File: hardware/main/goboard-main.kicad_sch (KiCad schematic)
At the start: 11 parts, among them J1 USB_C_Receptacle_USB2.0, J2 Conn_02x05_Top_Bottom, J3 Conn_01x01, J4 Conn_01x04, SW11 SW_Push, SW30 SW_DP3T

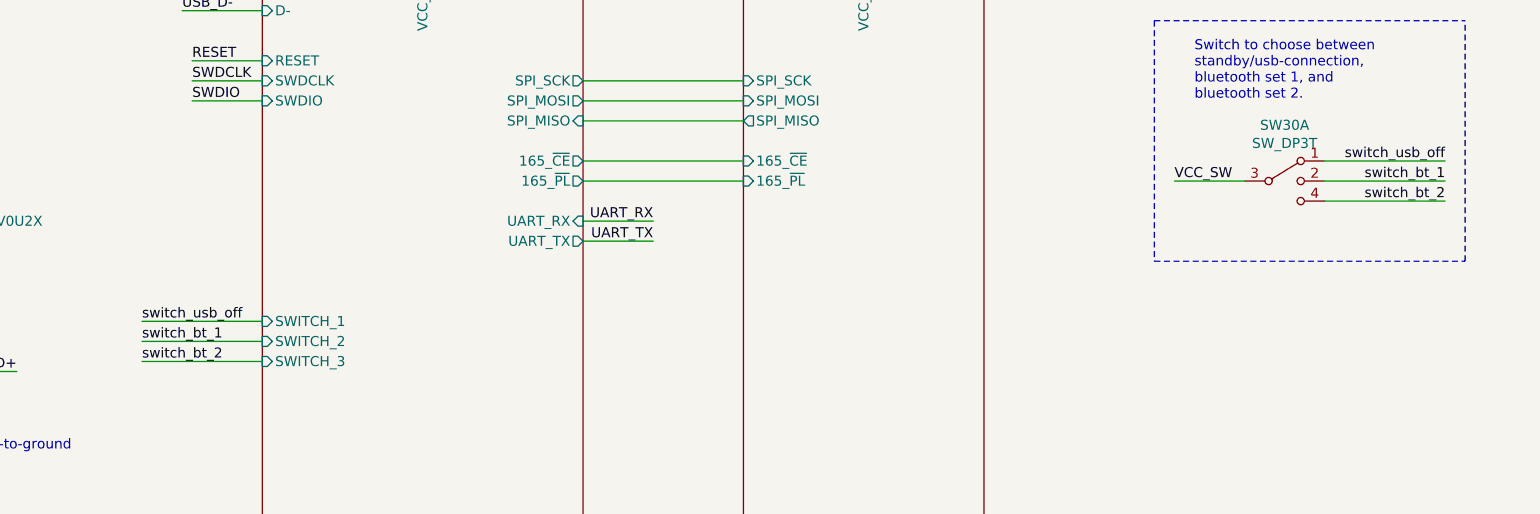
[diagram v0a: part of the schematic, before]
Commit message: Rework the off/bluetooth1/bluetooth2 switch connection
To save energy an external pull-down resistor is added and the off
position is not connected to the MCU.
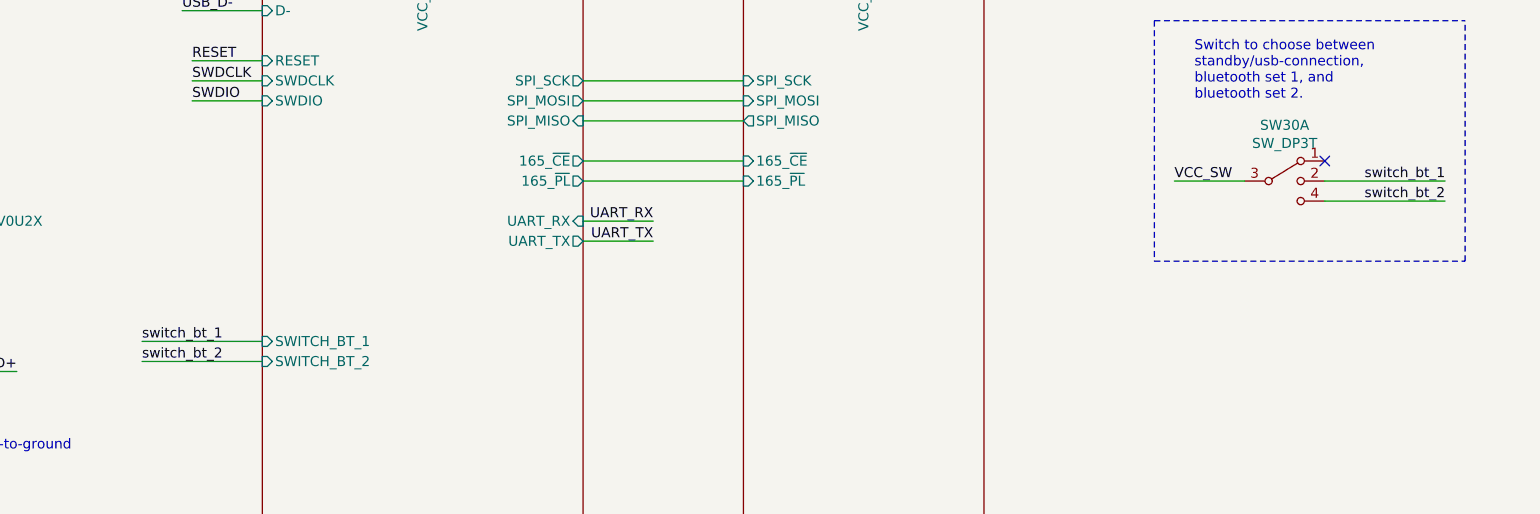
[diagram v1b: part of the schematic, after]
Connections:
- net switch_usb_off: no longer names the net of SW30.1
- no-connect marks 5 -> 6
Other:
- sheet MCU ports: added SWITCH_BT_1, SWITCH_BT_2; removed SWITCH_1, SWITCH_2, SWITCH_3
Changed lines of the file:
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@@
   (no_connect (at 41.91 66.04))
   (no_connect (at 45.72 165.1))
+  (no_connect (at 255.27 64.77))
   (wire (pts (xy 19.05 73.66) (xy 19.05 76.2))
     (stroke (width 0) (type solid) (color 0 0 0 0))
@@
     (stroke (width 0) (type solid) (color 0 0 0 0))
   )
-  (wire (pts (xy 105.41 85.09) (xy 120.65 85.09))
-    (stroke (width 0) (type solid) (color 0 0 0 0))
-  )
   (wire (pts (xy 105.41 87.63) (xy 120.65 87.63))
     (stroke (width 0) (type solid) (color 0 0 0 0))
@@
   )
   (wire (pts (xy 250.19 139.7) (xy 260.35 139.7))
-    (stroke (width 0) (type solid) (color 0 0 0 0))
-  )
-  (wire (pts (xy 255.27 64.77) (xy 270.51 64.77))
     (stroke (width 0) (type solid) (color 0 0 0 0))
   )
@@
     (effects (font (size 1.27 1.27)) (justify right bottom))
   )
-  (label "switch_usb_off" (at 105.41 85.09 0)
-    (effects (font (size 1.27 1.27)) (justify left bottom))
-  )
   (label "switch_bt_1" (at 105.41 87.63 0)
     (effects (font (size 1.27 1.27)) (justify left bottom))
@@
   (label "UART_TX" (at 250.19 139.7 0)
     (effects (font (size 1.27 1.27)) (justify left bottom))
-  )
-  (label "switch_usb_off" (at 270.51 64.77 180)
-    (effects (font (size 1.27 1.27)) (justify right bottom))
   )
   (label "switch_bt_1" (at 270.51 67.31 180)
@@
       (effects (font (size 1.27 1.27)) (justify right))
     )
-    (pin "SWITCH_1" input (at 120.65 85.09 180)
-      (effects (font (size 1.27 1.27)) (justify left))
-    )
-    (pin "SWITCH_2" input (at 120.65 87.63 180)
-      (effects (font (size 1.27 1.27)) (justify left))
-    )
-    (pin "SWITCH_3" input (at 120.65 90.17 180)
-      (effects (font (size 1.27 1.27)) (justify left))
-    )
     (pin "V_MID" input (at 120.65 111.76 180)
       (effects (font (size 1.27 1.27)) (justify left))
@@
     )
     (pin "CHARGE" output (at 120.65 134.62 180)
+      (effects (font (size 1.27 1.27)) (justify left))
+    )
+    (pin "SWITCH_BT_2" input (at 120.65 90.17 180)
+      (effects (font (size 1.27 1.27)) (justify left))
+    )
+    (pin "SWITCH_BT_1" input (at 120.65 87.63 180)
       (effects (font (size 1.27 1.27)) (justify left))
     )
@@
       (reference "#PWR0147") (unit 1) (value "+5V") (footprint "")
     )
+    (path "/d1d7b976-c206-4a6a-bf43-9e0a3d3fc0a5/cf9f8d8d-da0f-4591-b106-4ccbc5c13dc0"
+      (reference "#PWR0148") (unit 1) (value "GND") (footprint "")
+    )
+    (path "/d1d7b976-c206-4a6a-bf43-9e0a3d3fc0a5/020d5d8f-9949-4018-bf6f-14d0c6edcb95"
+      (reference "#PWR?") (unit 1) (value "GND") (footprint "")
+    )
     (path "/d1d7b976-c206-4a6a-bf43-9e0a3d3fc0a5/3b11a76b-0594-44ea-a5af-67b22af13aef"
       (reference "C1") (unit 1) (value "100nF") (footprint "Capacitor_SMD:C_0603_1608Metric_Pad1.08x0.95mm_HandSolder")
@@
       (reference "R24") (unit 1) (value "100k") (footprint "Resistor_SMD:R_0603_1608Metric_Pad0.98x0.95mm_HandSolder")
     )
+    (path "/d1d7b976-c206-4a6a-bf43-9e0a3d3fc0a5/f9d78325-6fa2-4c37-ba1e-b9fa566c985f"
+      (reference "R25") (unit 1) (value "100k") (footprint "Resistor_SMD:R_0603_1608Metric_Pad0.98x0.95mm_HandSolder")
+    )
+    (path "/d1d7b976-c206-4a6a-bf43-9e0a3d3fc0a5/3a9f3330-4728-47be-a54c-1662ecaf0122"
+      (reference "R26") (unit 1) (value "100k") (footprint "Resistor_SMD:R_0603_1608Metric_Pad0.98x0.95mm_HandSolder")
+    )
     (path "/d1d7b976-c206-4a6a-bf43-9e0a3d3fc0a5/ab5a7c2d-c6f5-4633-a330-435b31021904"

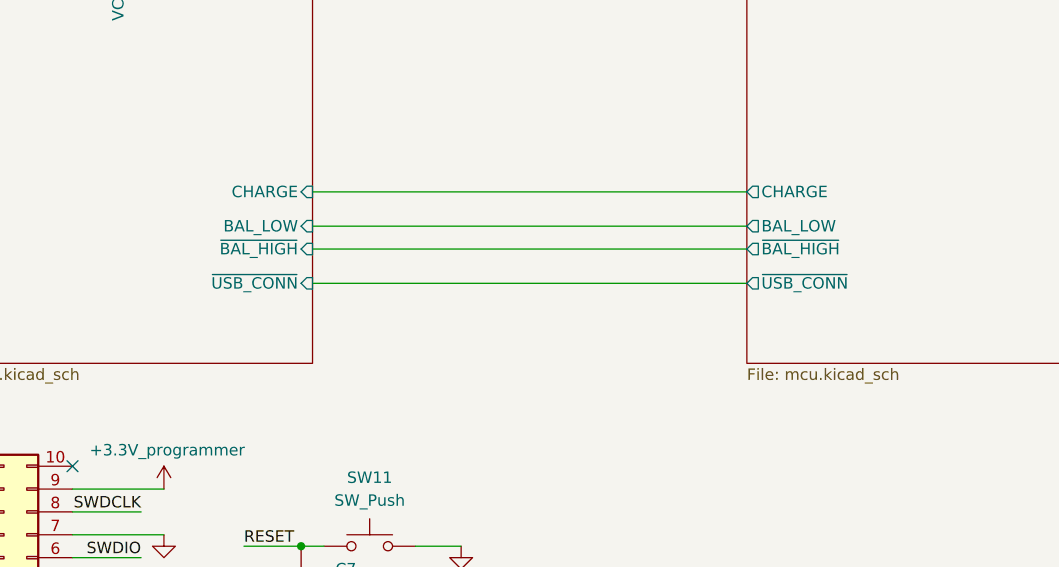
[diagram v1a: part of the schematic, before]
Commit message: Remove the USB sense curcuit
As V_BUS is connected to the MCU it can detect when the USB is
connected.
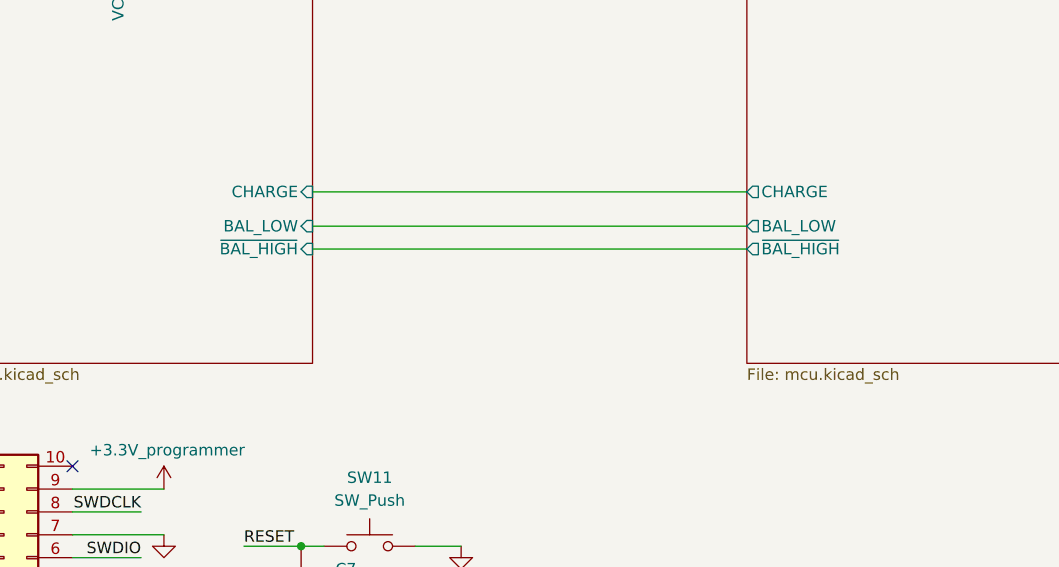
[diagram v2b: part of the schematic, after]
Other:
- sheet MCU ports: added none; removed ~USB_CONN
- sheet Power Supply ports: added none; removed ~USB_CONN
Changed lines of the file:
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@@
-    (stroke (width 0) (type solid) (color 0 0 0 0))
-  )
-  (wire (pts (xy 72.39 144.78) (xy 120.65 144.78))
     (stroke (width 0) (type solid) (color 0 0 0 0))
   )
@@
       (effects (font (size 1.27 1.27)) (justify left))
     )
-    (pin "~USB_CONN" output (at 120.65 144.78 180)
-      (effects (font (size 1.27 1.27)) (justify left))
-    )
     (pin "CHARGE" output (at 120.65 134.62 180)
       (effects (font (size 1.27 1.27)) (justify left))
@@
       (effects (font (size 1.27 1.27)) (justify right))
     )
-    (pin "~USB_CONN" input (at 72.39 144.78 0)
-      (effects (font (size 1.27 1.27)) (justify right))
-    )
     (pin "VCC_SW" output (at 50.8 106.68 90)
       (effects (font (size 1.27 1.27)) (justify right))
@@
     )
     (path "/d1d7b976-c206-4a6a-bf43-9e0a3d3fc0a5/020d5d8f-9949-4018-bf6f-14d0c6edcb95"
-      (reference "#PWR?") (unit 1) (value "GND") (footprint "")
+      (reference "#PWR0149") (unit 1) (value "GND") (footprint "")
     )
     (path "/d1d7b976-c206-4a6a-bf43-9e0a3d3fc0a5/3b11a76b-0594-44ea-a5af-67b22af13aef"
@@
       (reference "#PWR0139") (unit 1) (value "GND") (footprint "")
     )
-    (path "/a2ebbcc0-d455-4794-9fcf-d50cef56d65b/823cf678-f342-46a9-bc13-64c57b402a88"
-      (reference "#PWR0140") (unit 1) (value "+3.3V") (footprint "")
-    )
-    (path "/a2ebbcc0-d455-4794-9fcf-d50cef56d65b/e04f67f3-0845-4fac-a587-d14754b2050a"
-      (reference "#PWR0141") (unit 1) (value "GND") (footprint "")
-    )
     (path "/a2ebbcc0-d455-4794-9fcf-d50cef56d65b/210515f0-c0f1-4f80-b920-f3ce9df10676"
       (reference "BT1") (unit 1) (value "NiMH") (footprint "Connector_PinHeader_2.54mm:PinHeader_1x02_P2.54mm_Horizontal")
@@
       (reference "Q7") (unit 1) (value "BC817") (footprint "Package_TO_SOT_SMD:SOT-23")
     )
-    (path "/a2ebbcc0-d455-4794-9fcf-d50cef56d65b/c0066439-6f06-4a67-928e-bc8b537c0ae3"
-      (reference "Q8") (unit 1) (value "BC817") (footprint "Package_TO_SOT_SMD:SOT-23")
-    )
     (path "/a2ebbcc0-d455-4794-9fcf-d50cef56d65b/94b1480c-21b6-4ef7-b592-3977ba8ffc39"
       (reference "R7") (unit 1) (value "10K") (footprint "Resistor_SMD:R_0603_1608Metric")
@@
       (reference "R18") (unit 1) (value "30") (footprint "Resistor_SMD:R_0603_1608Metric")
     )
-    (path "/a2ebbcc0-d455-4794-9fcf-d50cef56d65b/77e371f3-d71f-42e5-8d23-cb2ab25eedc7"
-      (reference "R19") (unit 1) (value "4.7K") (footprint "Resistor_SMD:R_0603_1608Metric")
-    )
-    (path "/a2ebbcc0-d455-4794-9fcf-d50cef56d65b/0e9703f0-097e-4788-98c6-20d860ee2991"
-      (reference "R20") (unit 1) (value "10K") (footprint "Resistor_SMD:R_0603_1608Metric")
-    )
     (path "/a2ebbcc0-d455-4794-9fcf-d50cef56d65b/78c02ca2-aa30-4480-8ca6-63a644f03ebe"

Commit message: Add circuit to disconnect the shift registers
This is done to save energy when the keyboard is switched off.
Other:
- sheet MCU ports: added ~ENABLE_VCC_KEYS; removed none
- sheet Power Supply ports: added VCC_KEYS, ~ENABLE_VCC_KEYS; removed none
- sheet keys ports: added VCC_KEYS; removed VCC_SW
- note removed: "TODO: possibility to switch of the power supply of the shift registers"
- note removed: "TODO: read the battery voltage with the MCU"
- note removed: "TODO: switch for pairing"
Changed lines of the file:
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@@
+    (stroke (width 0) (type solid) (color 0 0 0 0))
+  )
+  (wire (pts (xy 62.23 104.14) (xy 62.23 106.68))
     (stroke (width 0) (type solid) (color 0 0 0 0))
   )
@@
     (stroke (width 0) (type solid) (color 0 0 0 0))
   )
+  (wire (pts (xy 72.39 130.81) (xy 120.65 130.81))
+    (stroke (width 0) (type solid) (color 0 0 0 0))
+  )
   (wire (pts (xy 72.39 134.62) (xy 120.65 134.62))
     (stroke (width 0) (type solid) (color 0 0 0 0))
@@
     (stroke (width 0) (type solid) (color 0 0 0 0))
   )
+  (wire (pts (xy 73.66 104.14) (xy 62.23 104.14))
+    (stroke (width 0) (type solid) (color 0 0 0 0))
+  )
   (wire (pts (xy 80.01 71.12) (xy 80.01 91.44))
     (stroke (width 0) (type solid) (color 0 0 0 0))
@@
     (stroke (width 0) (type solid) (color 0 0 0 0))
   )
-  (wire (pts (xy 196.85 36.83) (xy 205.74 36.83))
+  (wire (pts (xy 196.85 36.83) (xy 208.28 36.83))
     (stroke (width 0) (type solid) (color 0 0 0 0))
   )
@@
     (effects (font (size 1.27 1.27)) (justify left bottom))
   )
-  (text "TODO: switch for pairing" (at 116.84 22.86 180)
-    (effects (font (size 1.27 1.27)) (justify right bottom))
-  )
-  (text "TODO: read the battery voltage with the MCU" (at 137.16 27.94 180)
-    (effects (font (size 1.27 1.27)) (justify right bottom))
-  )
-  (text "TODO: possibility to switch of the\npower supply of the shift registers"
-    (at 215.9 30.48 0)
-    (effects (font (size 1.27 1.27)) (justify right bottom))
-  )
   (text "Switch to choose between\nstandby/usb-connection,\nbluetooth set 1, and\nbluetooth set 2."
     (at 238.76 57.15 0)
@@
     (effects (font (size 1.27 1.27)) (justify left bottom))
   )
+  (label "VCC_KEYS" (at 73.66 104.14 180)
+    (effects (font (size 1.27 1.27)) (justify right bottom))
+  )
   (label "USB_D+" (at 89.535 91.44 180)
     (effects (font (size 1.27 1.27)) (justify right bottom))
@@
     (effects (font (size 1.27 1.27)) (justify right bottom))
   )
-  (label "VCC_SW" (at 205.74 36.83 180)
+  (label "VCC_KEYS" (at 208.28 36.83 180)
     (effects (font (size 1.27 1.27)) (justify right bottom))
   )
@@
       (effects (font (size 1.27 1.27)) (justify left))
     )
+    (pin "~ENABLE_VCC_KEYS" output (at 120.65 130.81 180)
+      (effects (font (size 1.27 1.27)) (justify left))
+    )
   )
   (sheet (at 27.94 106.68) (size 44.45 46.99)
@@
       (effects (font (size 1.27 1.27)) (justify right))
     )
+    (pin "VCC_KEYS" output (at 62.23 106.68 90)
+      (effects (font (size 1.27 1.27)) (justify right))
+    )
+    (pin "~ENABLE_VCC_KEYS" input (at 72.39 130.81 0)
+      (effects (font (size 1.27 1.27)) (justify right))
+    )
   )
   (sheet (at 181.61 39.37) (size 30.48 107.7976)
@@
       (effects (font (size 1.27 1.27)) (justify left))
     )
-    (pin "VCC_SW" input (at 196.85 39.37 90)
+    (pin "VCC_KEYS" input (at 196.85 39.37 90)
       (effects (font (size 1.27 1.27)) (justify right))
     )
@@
       (reference "#PWR0121") (unit 1) (value "GND") (footprint "")
     )
-    (path "/d1d7b976-c206-4a6a-bf43-9e0a3d3fc0a5/ac41e8bc-33f1-480a-9578-3f27442f4e39"
-      (reference "#PWR0122") (unit 1) (value "GND") (footprint "")
-    )
-    (path "/d1d7b976-c206-4a6a-bf43-9e0a3d3fc0a5/456c5560-5e5c-458e-a7f7-e577da6fbd17"
-      (reference "#PWR0123") (unit 1) (value "GND") (footprint "")
-    )
     (path "/d1d7b976-c206-4a6a-bf43-9e0a3d3fc0a5/5d0f01e6-3cac-4a3c-9bd2-0ba422ba5ad9"
       (reference "#PWR0124") (unit 1) (value "GND") (footprint "")
@@
       (reference "U4") (unit 1) (value "74LV165") (footprint "Package_SO:TSSOP-16_4.4x5mm_P0.65mm")
     )
+    (path "/a2ebbcc0-d455-4794-9fcf-d50cef56d65b/c13ba79c-ae64-4b9d-8123-a7ed738a1064"
+      (reference "#PWR0122") (unit 1) (value "GND") (footprint "")
+    )
     (path "/a2ebbcc0-d455-4794-9fcf-d50cef56d65b/481ca36e-2d56-4ed3-8c05-f65e606c1b2f"
       (reference "#PWR0125") (unit 1) (value "GND") (footprint "")
@@
       (reference "Q7") (unit 1) (value "BC817") (footprint "Package_TO_SOT_SMD:SOT-23")
     )
+    (path "/a2ebbcc0-d455-4794-9fcf-d50cef56d65b/c2e8ebbb-bf40-443d-9bf3-873700b3381d"
+      (reference "Q8") (unit 1) (value "SSM3J338R") (footprint "Package_TO_SOT_SMD:SOT-23_Handsoldering")
+    )
     (path "/a2ebbcc0-d455-4794-9fcf-d50cef56d65b/94b1480c-21b6-4ef7-b592-3977ba8ffc39"
       (reference "R7") (unit 1) (value "10K") (footprint "Resistor_SMD:R_0603_1608Metric")
@@
       (reference "R18") (unit 1) (value "30") (footprint "Resistor_SMD:R_0603_1608Metric")
     )
+    (path "/a2ebbcc0-d455-4794-9fcf-d50cef56d65b/0c97694b-516e-4ec3-b4a1-2fae81dd0262"
+      (reference "R19") (unit 1) (value "10K") (footprint "Resistor_SMD:R_0603_1608Metric")
+    )
     (path "/a2ebbcc0-d455-4794-9fcf-d50cef56d65b/78c02ca2-aa30-4480-8ca6-63a644f03ebe"
